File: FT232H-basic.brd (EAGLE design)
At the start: 45.7 x 17.8 mm, 29 parts, among them IC1 FT232H

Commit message: board passes ERC
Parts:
- C1: value (none) -> 0.1uF
- L1: value (none) -> 600R/500ma
- USB1: value (none) -> USB-MINI-AB-TH-MOLEX-SLOT
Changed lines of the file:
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@@
 <attribute name="VALUE" x="10.6172" y="19.1516" size="0.4064" layer="27" font="vector" rot="R90"/>
 </element>
-<element name="USB1" library="USB-Mini-Molex" package="USB-MINI-AB-TH-MOLEX-SLOT" value="" x="12.6238" y="13.9446" smashed="yes">
+<element name="USB1" library="USB-Mini-Molex" package="USB-MINI-AB-TH-MOLEX-SLOT" value="USB-MINI-AB-TH-MOLEX-SLOT" x="12.6238" y="13.9446" smashed="yes">
 <attribute name="NAME" x="14.9606" y="9.6266" size="0.6096" layer="25" font="vector" ratio="10" rot="R90"/>
 <attribute name="VALUE" x="7.5438" y="11.4046" size="0.4064" layer="27" font="vector" rot="R90"/>
@@
 <attribute name="VALUE" x="17.3228" y="16.3322" size="0.4064" layer="27" font="vector"/>
 </element>
-<element name="L1" library="SparkFun-Passives" package="0603" value="" x="21.844" y="17.4752" smashed="yes">
+<element name="L1" library="SparkFun-Passives" package="0603" value="600R/500ma" x="21.844" y="17.4752" smashed="yes">
 <attribute name="NAME" x="21.463" y="15.9512" size="0.6096" layer="25" font="vector" ratio="10"/>
 <attribute name="VALUE" x="20.828" y="16.3322" size="0.4064" layer="27" font="vector"/>
 </element>
-<element name="C1" library="SparkFun-Passives" package="0603-CAP" value="" x="21.8694" y="18.9484" smashed="yes">
+<element name="C1" library="SparkFun-Passives" package="0603-CAP" value="0.1uF" x="21.8694" y="18.9484" smashed="yes">
 <attribute name="NAME" x="21.4884" y="19.6088" size="0.6096" layer="25" font="vector" ratio="10"/>
 <attribute name="VALUE" x="20.8534" y="17.8054" size="0.4064" layer="27" font="vector"/>

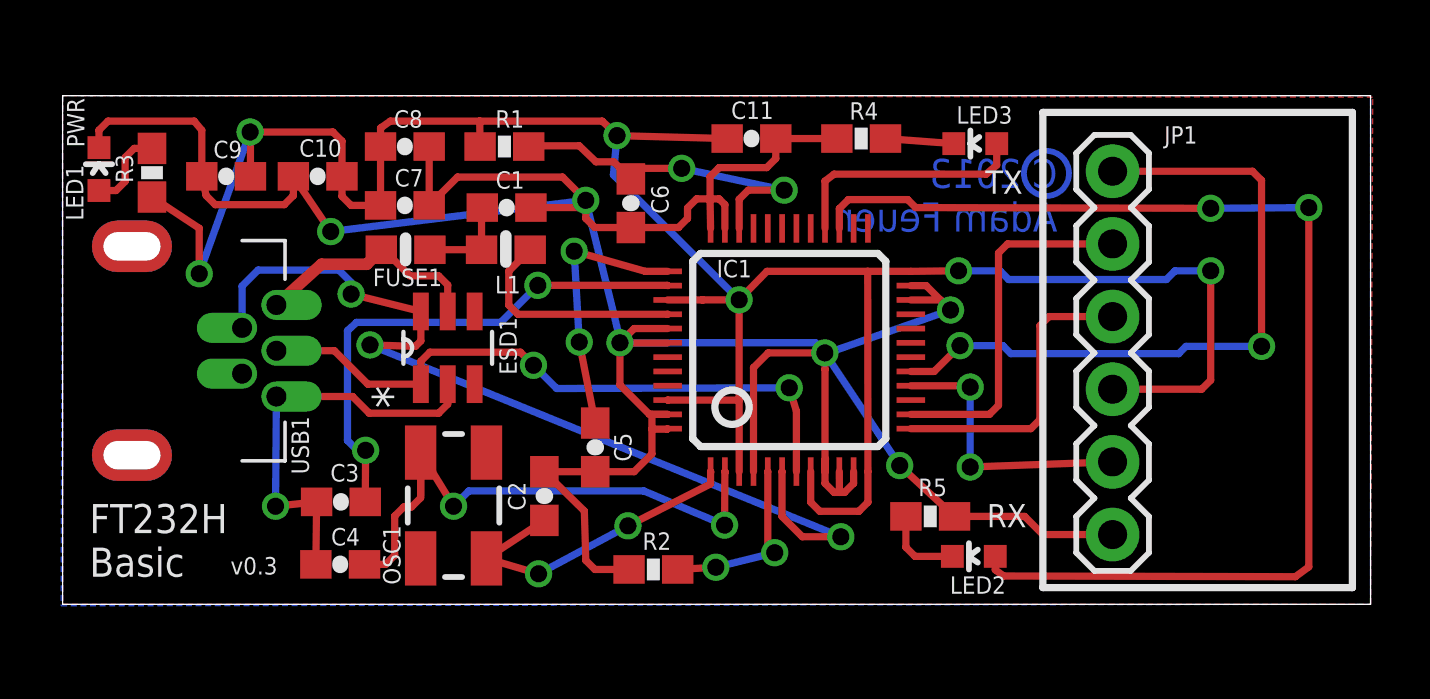
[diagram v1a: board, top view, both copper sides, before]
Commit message: minor changes to silkscreen
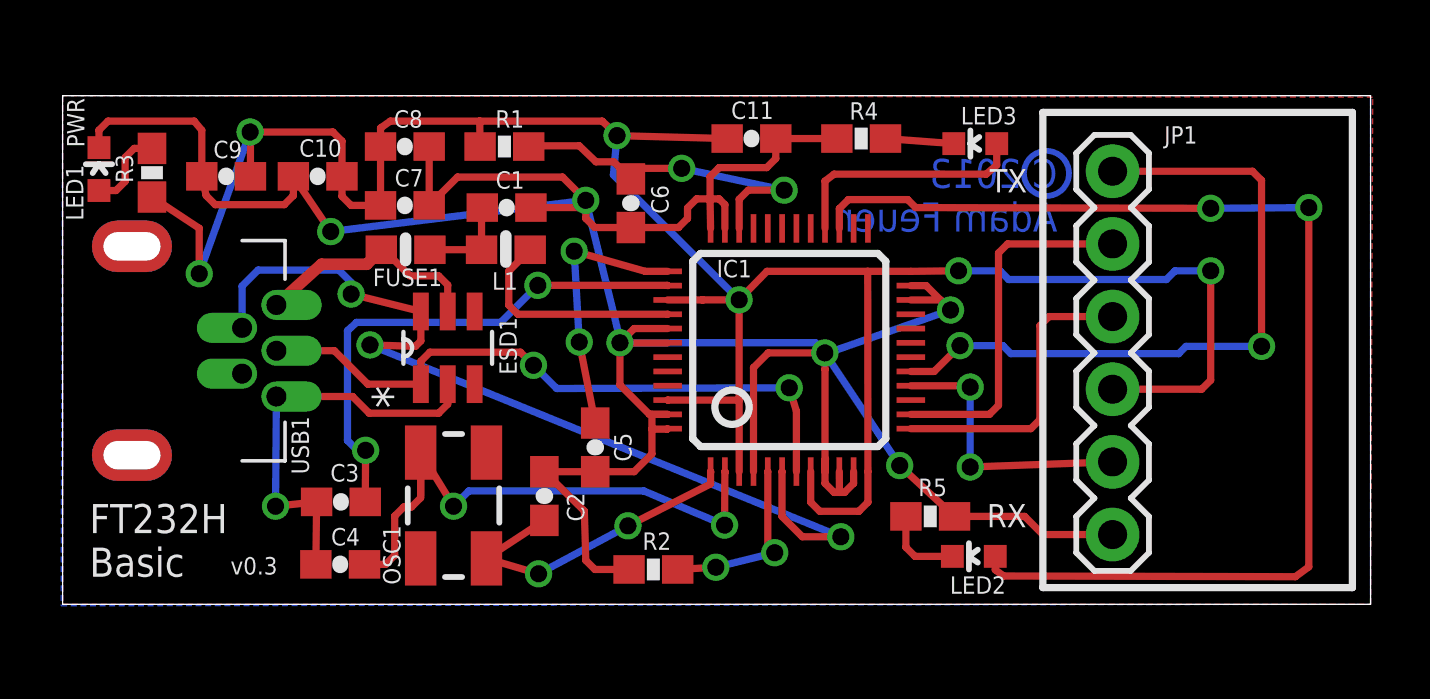
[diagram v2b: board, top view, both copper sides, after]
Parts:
- moved U$1 0.21 mm to (19.7, 18.7)
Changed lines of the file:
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@@
 <layer number="14" name="Route14" color="1" fill="6" visible="no" active="no"/>
 <layer number="15" name="Route15" color="4" fill="6" visible="no" active="no"/>
-<layer number="16" name="Bottom" color="1" fill="1" visible="yes" active="yes"/>
+<layer number="16" name="Bottom" color="1" fill="1" visible="no" active="yes"/>
 <layer number="17" name="Pads" color="2" fill="1" visible="yes" active="yes"/>
 <layer number="18" name="Vias" color="2" fill="1" visible="yes" active="yes"/>
@@
 <layer number="20" name="Dimension" color="15" fill="1" visible="yes" active="yes"/>
 <layer number="21" name="tPlace" color="7" fill="1" visible="yes" active="yes"/>
-<layer number="22" name="bPlace" color="7" fill="1" visible="yes" active="yes"/>
+<layer number="22" name="bPlace" color="7" fill="1" visible="no" active="yes"/>
 <layer number="23" name="tOrigins" color="15" fill="1" visible="yes" active="yes"/>
-<layer number="24" name="bOrigins" color="15" fill="1" visible="yes" active="yes"/>
+<layer number="24" name="bOrigins" color="15" fill="1" visible="no" active="yes"/>
 <layer number="25" name="tNames" color="7" fill="1" visible="yes" active="yes"/>
-<layer number="26" name="bNames" color="7" fill="1" visible="yes" active="yes"/>
+<layer number="26" name="bNames" color="7" fill="1" visible="no" active="yes"/>
 <layer number="27" name="tValues" color="7" fill="1" visible="no" active="yes"/>
 <layer number="28" name="bValues" color="7" fill="1" visible="no" active="yes"/>
@@
 <text x="41.1226" y="18.1102" size="1.016" layer="16" font="vector" ratio="20" rot="MR0">C 2013
 Adam Feuer</text>
-<text x="46.4566" y="21.4122" size="1.016" layer="22" font="vector" ratio="10" rot="MR0">Open Source Hardware</text>
-<text x="22.4282" y="5.5372" size="0.508" layer="22" font="vector" ratio="10" rot="MR0">Released under Creative Commons
-By-Attribution Share-Alike 3.0 license</text>
-<text x="38.608" y="19.431" size="0.8128" layer="21" font="vector">TX</text>
+<text x="47.1424" y="21.209" size="1.016" layer="22" font="vector" ratio="10" rot="MR0">Open Source Hardware</text>
+<text x="21.7932" y="5.7658" size="0.508" layer="22" font="vector" ratio="10" rot="MR0">Released under Creative Commons
+By-Attribution Share-Alike 3.0
+license</text>
+<text x="38.7604" y="19.4818" size="0.8128" layer="21" font="vector">TX</text>
 <text x="38.6588" y="7.7724" size="0.8128" layer="21" font="vector">RX</text>
 <text x="12.2174" y="6.1214" size="0.6096" layer="21" font="vector">v0.3</text>
@@
 <element name="C2" library="SparkFun-Capacitors" package="0603-CAP" value="27pF" x="23.1902" y="8.8646" smashed="yes" rot="R90">
 <attribute name="PROD_ID" value="CAP-08604" x="60.0202" y="46.9646" size="1.778" layer="27" rot="R90" display="off"/>
-<attribute name="NAME" x="22.5298" y="8.3566" size="0.6096" layer="25" font="vector" ratio="10" rot="R90"/>
+<attribute name="NAME" x="24.5872" y="7.9756" size="0.6096" layer="25" font="vector" ratio="10" rot="R90"/>
 <attribute name="VALUE" x="24.3332" y="7.8486" size="0.4064" layer="27" font="vector" rot="R90"/>
 </element>
@@
 <element name="LED3" library="SparkFun-LED" package="LED-0603" value="YELLOW" x="38.2524" y="21.1836" smashed="yes" rot="R90">
 <attribute name="PROD_ID" value="DIO-09003" x="75.0824" y="46.5836" size="1.778" layer="27" rot="R90" display="off"/>
-<attribute name="NAME" x="39.5478" y="22.4917" size="0.6096" layer="25" font="vector" ratio="10" rot="R180"/>
+<attribute name="NAME" x="39.7002" y="22.4663" size="0.6096" layer="25" font="vector" ratio="10" rot="R180"/>
 <attribute name="VALUE" x="39.2684" y="22.2631" size="0.4064" layer="27" rot="R180"/>
 </element>
@@
 </element>
 <element name="FRAME1" library="SparkFun-Aesthetics" package="CREATIVE_COMMONS" value="FRAME-LETTER" x="20.32" y="-7.62" smashed="yes"/>
-<element name="U$1" library="SparkFun-Aesthetics" package="OSHW-LOGO-L" value="" x="19.7866" y="18.8976" smashed="yes" rot="MR0"/>
+<element name="U$1" library="SparkFun-Aesthetics" package="OSHW-LOGO-L" value="" x="19.7358" y="18.6944" smashed="yes" rot="MR0"/>
 <element name="ESD1" library="NXP_By_element14_Batch_1" package="SOT95P275X110-6N" value="IP4220CZ6" x="19.812" y="14.0462" smashed="yes" rot="R90">
 <attribute name="PACKAGE" value="SSOT-6" x="19.812" y="14.0462" size="1.778" layer="27" rot="R90" display="off"/>
@@
 </element>
 <element name="L1" library="SparkFun-Passives" package="0603" value="600R/500ma" x="21.844" y="17.4752" smashed="yes">
-<attribute name="NAME" x="21.463" y="15.9512" size="0.6096" layer="25" font="vector" ratio="10"/>
+<attribute name="NAME" x="21.3614" y="16.0782" size="0.6096" layer="25" font="vector" ratio="10"/>
 <attribute name="VALUE" x="20.828" y="16.3322" size="0.4064" layer="27" font="vector"/>
 </element>

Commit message: rerouted USART traces to keep them on top side of board, shortened paths - for high speed routing
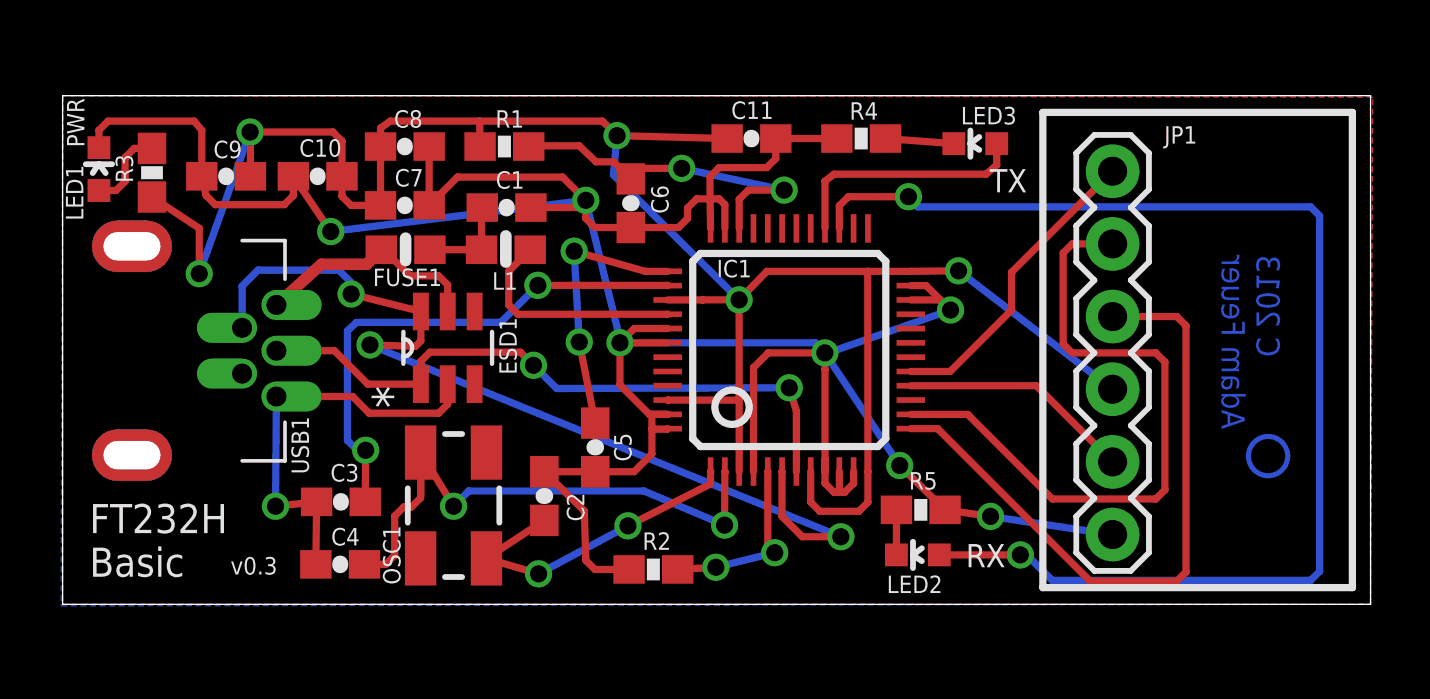
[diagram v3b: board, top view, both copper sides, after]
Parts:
- moved LED2 1.96 mm to (36.2, 6.81)
- moved R5 0.40 mm to (36.3, 8.38)
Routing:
- net DTR: track 24.0 -> 10.7 mm, vias 2 -> 0
- net TXO: track 10.6 -> 23.3 mm
- net RXI: track 12.6 -> 23.6 mm
- net POWER: track 87.7 -> 78.0 mm, vias 6 -> 5
- net RXLED: track 41.5 -> 44.2 mm
- net CTS: track 10.1 -> 8.16 mm, vias 2 -> 0
- net N$11: track 2.84 -> 1.57 mm
- net GND: track 127.6 -> 127.3 mm, vias 7 -> 8

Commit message: rerouted USB DP and DM traces to make them more direct - for high speed routing
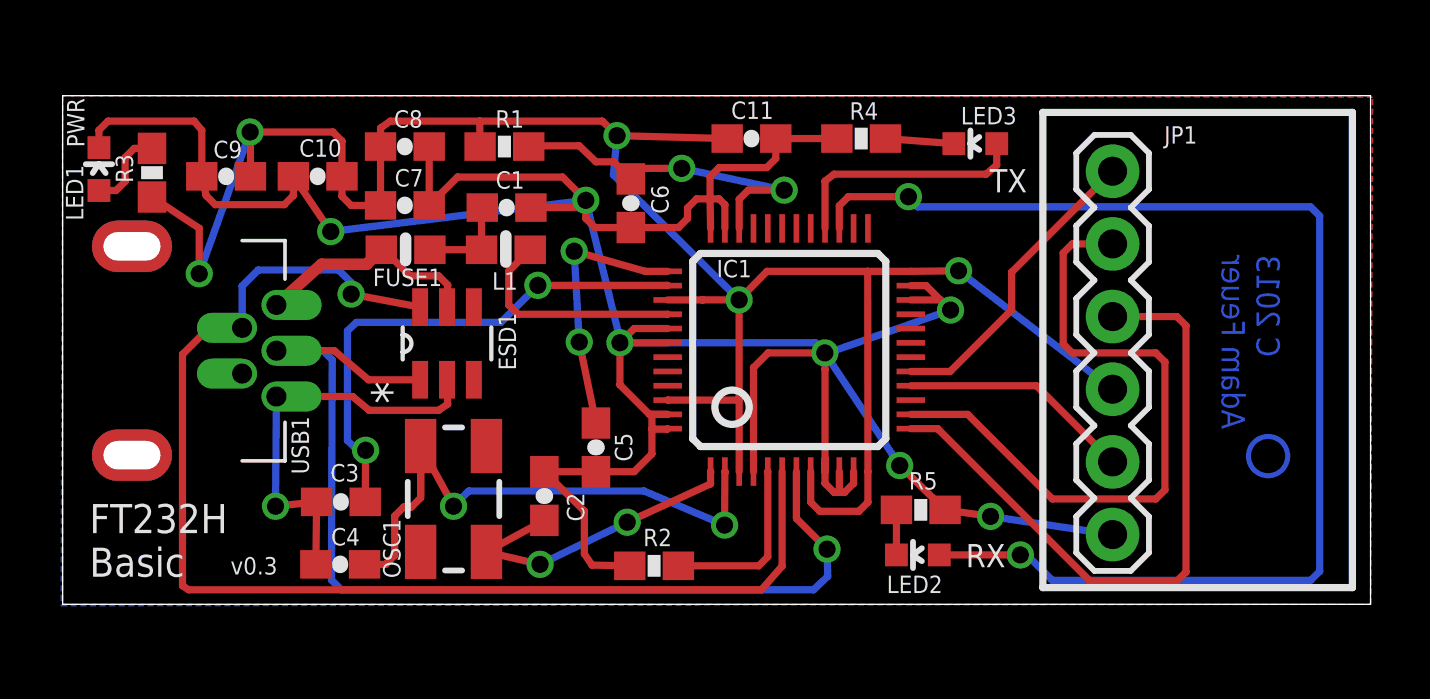
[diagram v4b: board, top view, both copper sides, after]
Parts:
- moved OSC1 0.23 mm to (20.0, 8.76)
- moved ESD1 0.15 mm to (19.8, 14.2)
- moved R2 0.13 mm to (27.0, 6.43)
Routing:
- net DP: track 22.8 -> 37.0 mm, vias 2 -> 1
- net DM: track 33.2 -> 43.8 mm, vias 3 -> 1
- net N$7: track 20.8 -> 21.5 mm
- net N$4: track 6.39 -> 6.23 mm, vias 2 -> 0

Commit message: rerouted USB DP and DM traces to be entirely on top of board, with shorter paths
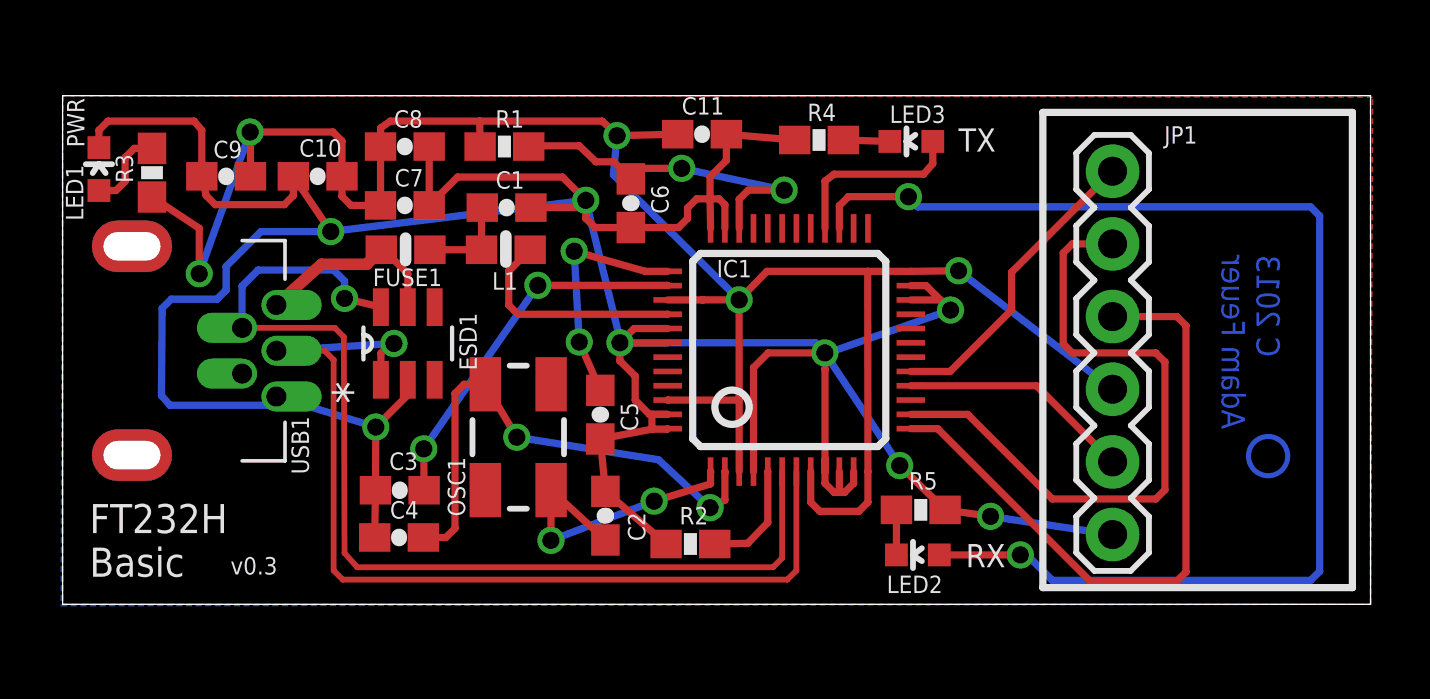
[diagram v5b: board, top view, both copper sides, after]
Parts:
- moved OSC1 3.13 mm to (22.3, 10.9)
- moved C4 2.26 mm to (18.1, 7.42)
- moved C2 2.24 mm to (25.3, 8.18)
- moved LED3 2.24 mm to (36.0, 21.3)
- moved C3 2.10 mm to (18.1, 9.07)
- moved C11 1.73 mm to (28.7, 21.5)
- moved R2 1.48 mm to (28.3, 7.19)
- moved R4 1.47 mm to (32.8, 21.3)
- moved ESD1 1.37 mm to (18.4, 14.2)
- moved C5 1.15 mm to (25.1, 11.7)
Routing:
- net DM: track 43.8 -> 37.3 mm
- net N$2: track 18.3 -> 13.0 mm
- net GND: track 127.3 -> 132.3 mm
- net N$7: track 21.5 -> 18.4 mm
- net N$4: track 6.23 -> 3.94 mm
- net TXLED: track 8.61 -> 6.45 mm
- net DP: track 37.0 -> 35.0 mm
- net POWER: track 78.0 -> 76.3 mm
- net VUSB: track 8.03 -> 6.86 mm
- net N$1: track 9.44 -> 8.39 mm
- net N$10: track 2.39 -> 1.63 mm
- net OSC1: track 11.3 -> 10.7 mm

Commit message: updated schematic to reflect correct size 0603 of FUSE1
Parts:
- FUSE1: value 1206L050YR Littelfuse -> 0603L050YR Littelfuse
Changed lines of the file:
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@@
 <attribute name="VALUE" x="39.878" y="21.4884" size="1.27" layer="27" rot="R270"/>
 </element>
-<element name="FUSE1" library="SparkFun-PowerIC" package="0603" value="1206L050YR Littelfuse" x="18.3388" y="17.4752" smashed="yes">
+<element name="FUSE1" library="SparkFun-PowerIC" package="0603" value="0603L050YR Littelfuse" x="18.3388" y="17.4752" smashed="yes">
 <attribute name="NAME" x="17.1958" y="16.2052" size="0.6096" layer="25" font="vector" ratio="10"/>
 <attribute name="VALUE" x="17.3228" y="16.3322" size="0.4064" layer="27" font="vector"/>
